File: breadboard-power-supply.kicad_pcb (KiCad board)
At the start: 2 copper layers, 34.8 x 55.2 mm, 17 parts, among them J1 Conn_01x02_Pin, J2 Conn_01x02_Pin, J3 Conn_01x03_Pin, J4 Conn_01x03_Pin, J5 Screw_Terminal_01x02, J6 Barrel_Jack_Switch, J7 Screw_Terminal_01x02, U1 LM7805_TO220, U2 LM317_TO-220

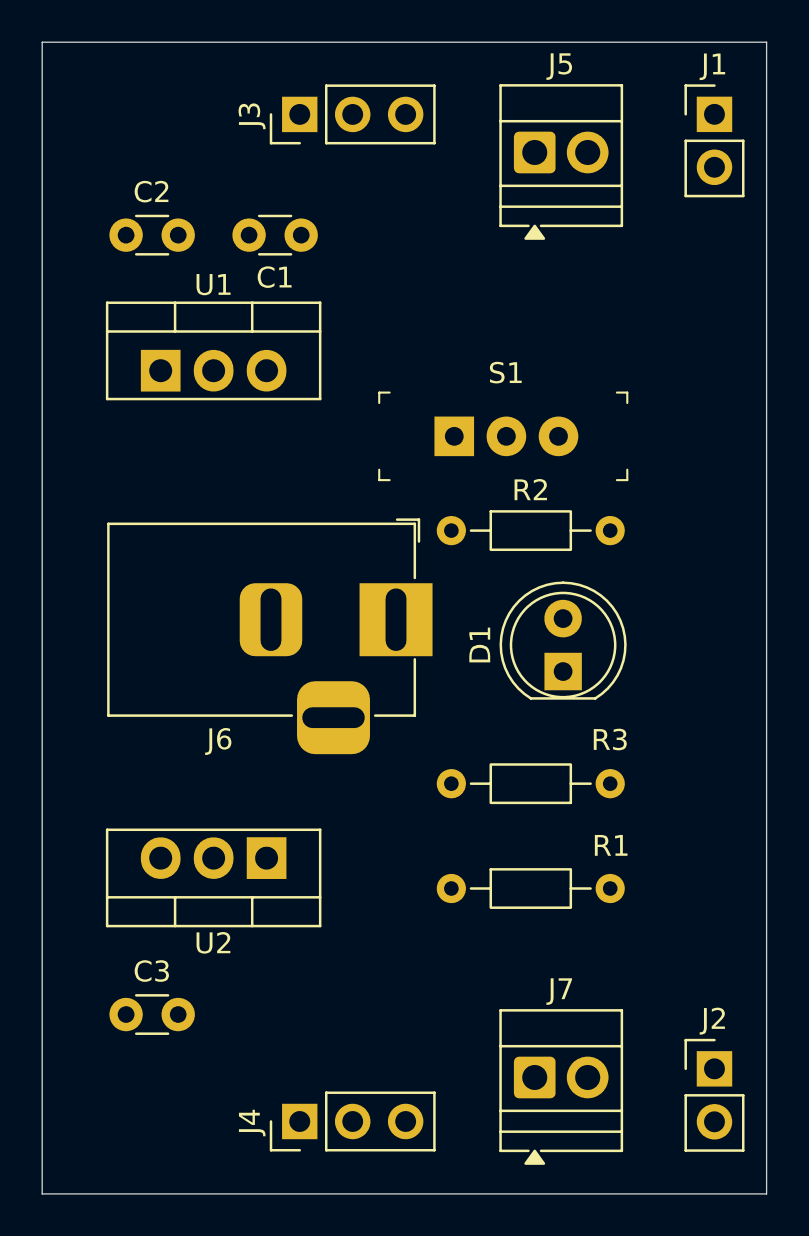
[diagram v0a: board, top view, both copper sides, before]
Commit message: PCB border refined
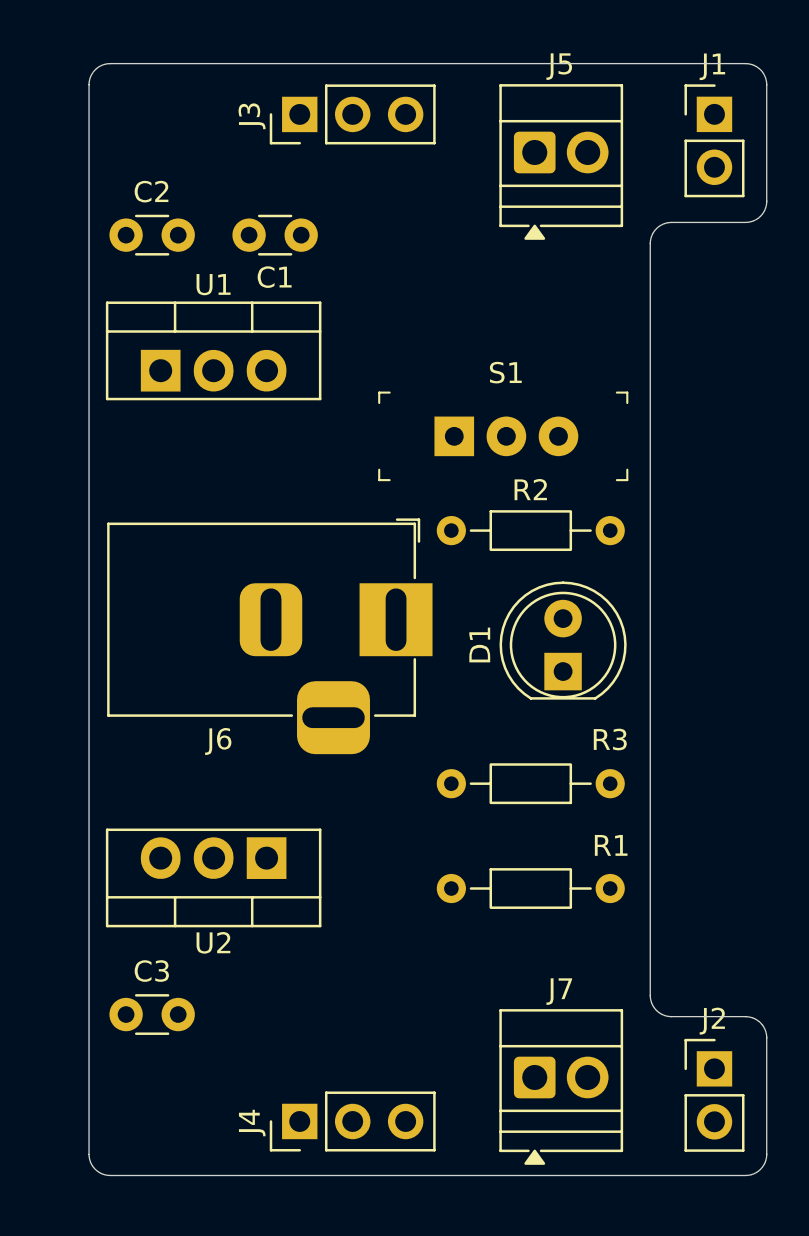
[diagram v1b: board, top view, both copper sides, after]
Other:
- board size 34.8 x 55.2 mm -> 32.5 x 53.3 mm
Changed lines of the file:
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@@
 		)
 		(property "Value" "Conn_01x02_Pin"
-			(at -3.6896 5.37 180)
+			(at -3.8928 -4.1296 180)
 			(layer "F.Fab")
 			(effects
@@
 		)
 		(property "Value" "Conn_01x02_Pin"
-			(at 0 4.92 0)
+			(at -3.6388 7.0656 0)
 			(layer "F.Fab")
 			(effects
@@
 		)
 	)
-	(gr_rect
-		(start 92.75 48.25)
-		(end 127.5 103.5)
+	(gr_line
+		(start 126.492 49.276)
+		(end 96.012 49.276)
+		(stroke
+			(width 0.05)
+			(type default)
+		)
+		(layer "Edge.Cuts")
+	)
+	(gr_arc
+		(start 122.936 94.996)
+		(mid 122.21758 94.69842)
+		(end 121.92 93.98)
+		(stroke
+			(width 0.05)
+			(type default)
+		)
+		(layer "Edge.Cuts")
+	)
+	(gr_arc
+		(start 121.92 57.912)
+		(mid 122.21758 57.19358)
+		(end 122.936 56.896)
+		(stroke
+			(width 0.05)
+			(type default)
+		)
+		(layer "Edge.Cuts")
+	)
+	(gr_line
+		(start 121.92 57.912)
+		(end 121.92 93.98)
+		(stroke
+			(width 0.05)
+			(type default)
+		)
+		(layer "Edge.Cuts")
+	)
+	(gr_line
+		(start 127.508 50.292)
+		(end 127.508 55.88)
+		(stroke
+			(width 0.05)
+			(type default)
+		)
+		(layer "Edge.Cuts")
+	)
+	(gr_line
+		(start 126.492 56.896)
+		(end 122.936 56.896)
+		(stroke
+			(width 0.05)
+			(type default)
+		)
+		(layer "Edge.Cuts")
+	)
+	(gr_arc
+		(start 126.492 49.276)
+		(mid 127.21042 49.57358)
+		(end 127.508 50.292)
+		(stroke
+			(width 0.05)
+			(type default)
+		)
+		(layer "Edge.Cuts")
+	)
+	(gr_line
+		(start 126.492 94.996)
+		(end 122.936 94.996)
+		(stroke
+			(width 0.05)
+			(type default)
+		)
+		(layer "Edge.Cuts")
+	)
+	(gr_line
+		(start 127.508 96.012)
+		(end 127.508 101.6)
+		(stroke
+			(width 0.05)
+			(type default)
+		)
+		(layer "Edge.Cuts")
+	)
+	(gr_line
+		(start 126.492 102.616)
+		(end 96.012 102.616)
+		(stroke
+			(width 0.05)
+			(type default)
+		)
+		(layer "Edge.Cuts")
+	)
+	(gr_arc
+		(start 127.508 101.6)
+		(mid 127.21042 102.31842)
+		(end 126.492 102.616)
+		(stroke
+			(width 0.05)
+			(type default)
+		)
+		(layer "Edge.Cuts")
+	)
+	(gr_arc
+		(start 126.492 94.996)
+		(mid 127.21042 95.29358)
+		(end 127.508 96.012)
+		(stroke
+			(width 0.05)
+			(type default)
+		)
+		(layer "Edge.Cuts")
+	)
+	(gr_arc
+		(start 94.996 50.292)
+		(mid 95.29358 49.57358)
+		(end 96.012 49.276)
+		(stroke
+			(width 0.05)
+			(type default)
+		)
+		(layer "Edge.Cuts")
+	)
+	(gr_arc
+		(start 96.012 102.616)
+		(mid 95.29358 102.31842)
+		(end 94.996 101.6)
+		(stroke
+			(width 0.05)
+			(type default)
+		)
+		(layer "Edge.Cuts")
+	)
+	(gr_arc
+		(start 127.508 55.88)
+		(mid 127.21042 56.59842)
+		(end 126.492 56.896)
+		(stroke
+			(width 0.05)
+			(type default)
+		)
+		(layer "Edge.Cuts")
+	)
+	(gr_line
+		(start 94.996 50.292)
+		(end 94.996 101.6)
 		(stroke
 			(width 0.05)
 			(type default)
 		)
-		(fill no)
 		(layer "Edge.Cuts")
 	)

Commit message: Routes
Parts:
- moved R1 7.78 mm to (120.1, 88.4), turned to 180 degrees
- moved R3 7.48 mm to (112.5, 83.8), turned to 0 degrees
- moved U1 5.28 mm to (103.6, 63.1), turned to 180 degrees
- moved S1 4.67 mm to (117.2, 67.1), turned to 180 degrees
- moved C2 2.52 mm to (99.3, 57.5), turned to 180 degrees
- moved C3 2.52 mm to (99.3, 94.9), turned to 180 degrees
- moved R2 0.09 mm to (112.3, 71.7)
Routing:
- net /PWR_OUTPUT: track 0.00 -> 89.8 mm
- net /3.3V: track 0.00 -> 76.5 mm, vias 0 -> 1
- net /5V: track 0.00 -> 61.8 mm
- net /12V: track 0.00 -> 58.3 mm
- net Net-(U2-ADJ): track 0.00 -> 22.5 mm
- net /PWR_INPUT: track 0.00 -> 11.0 mm
- net Net-(D1-A): track 0.00 -> 7.11 mm
- added copper zone on B.Cu, net GND

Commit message: Silkscreen
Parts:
- added REF**: KiCad-Logo2_5mm_SilkScreen, Symbol:KiCad-Logo2_5mm_SilkScreen, B.Cu at (108.2, 90.9)
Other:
- board text added: "+"
- board text added: "-"
- board text added: "3.3V"
- board text added: "5V"
- board text added: "Breadboard Power Suppy"
- board text added: "GND"
- board text added: "HanzeeLabs"
- board text added: "OFF"
- board text added: "ON"
- board text added: "v1.0.0"
